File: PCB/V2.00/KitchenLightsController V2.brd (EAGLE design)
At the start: 100 x 90 mm, 116 parts, among them IC1 788TV, Q2 FDD8451, Q3 FDD8451, Q4 FDD8451, Q5 FDD8451, Q6 200mA/50V, U1 PHOTON_WITH_STACKABLE_HEADERS, U2 DS1820SOIC, U3 ACS712

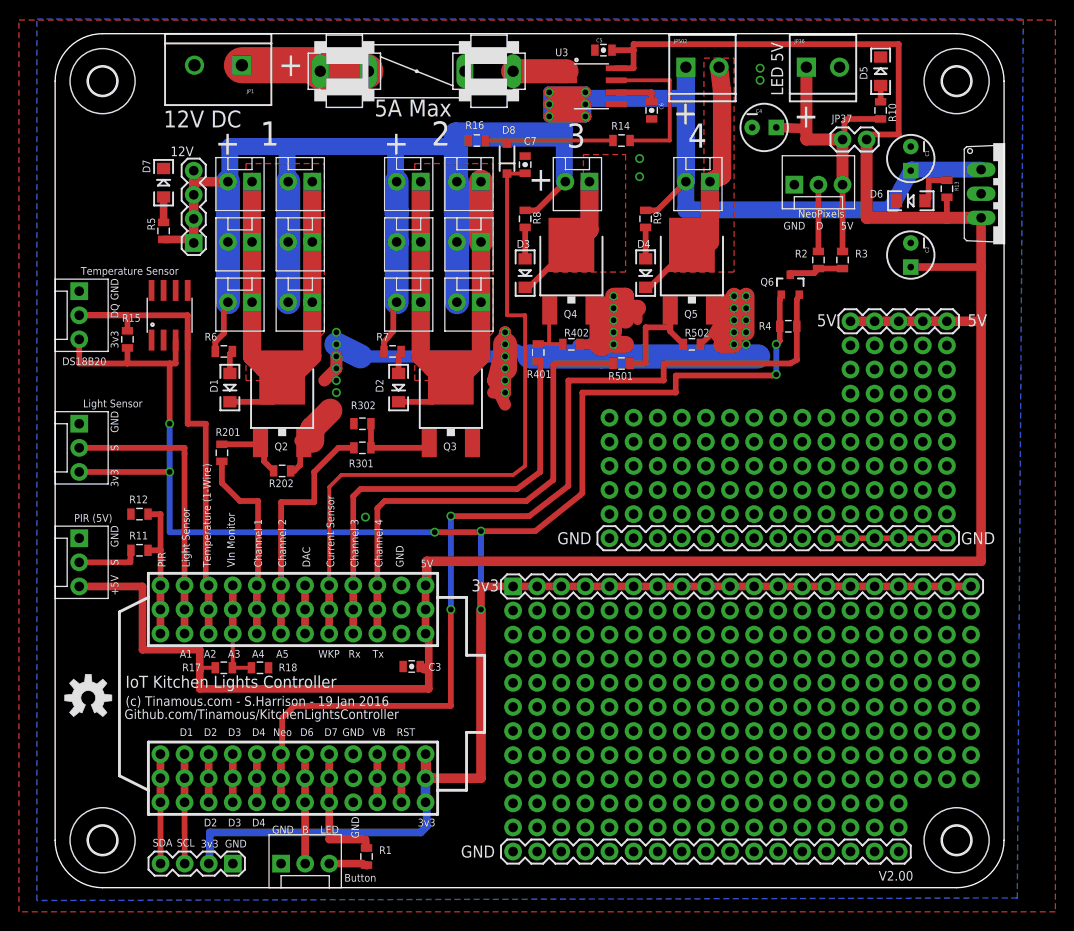
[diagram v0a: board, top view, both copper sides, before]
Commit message: Updated with minor tweaks and some additional component values specified from build of the v2.00 board.
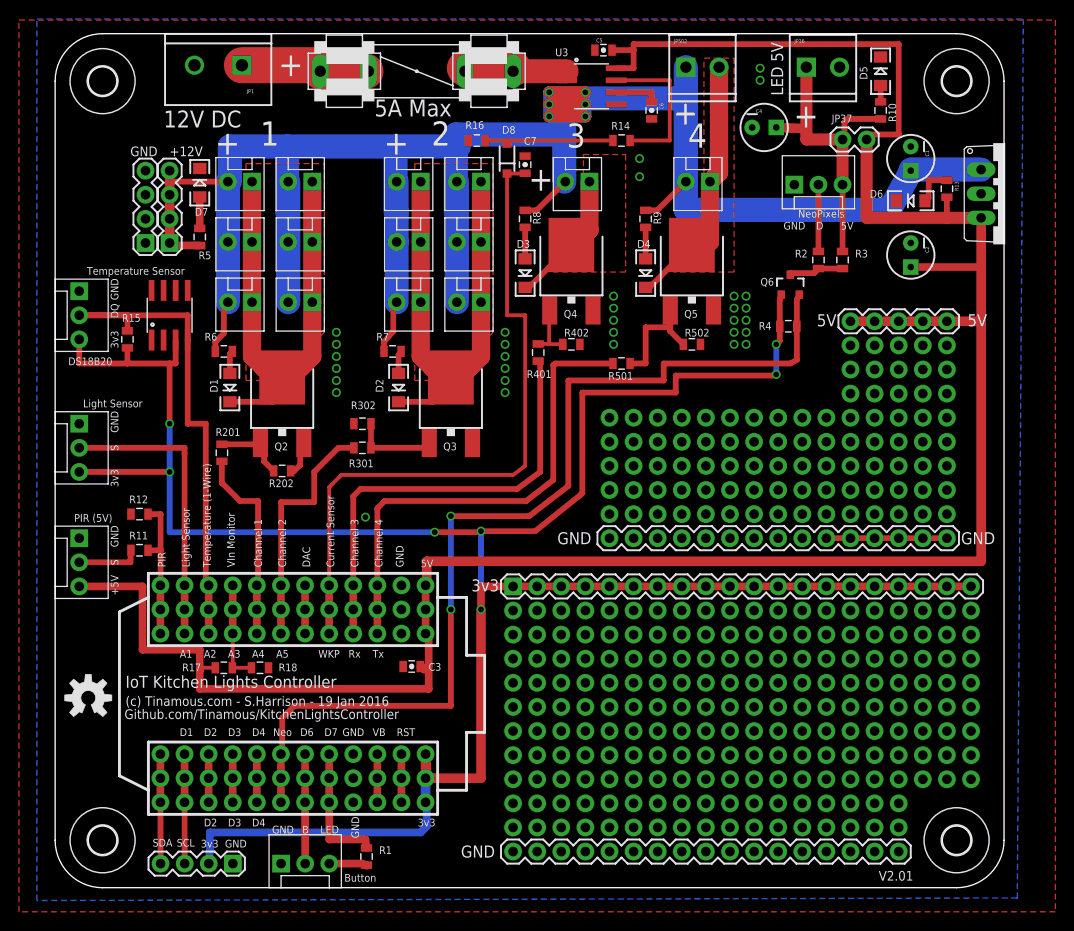
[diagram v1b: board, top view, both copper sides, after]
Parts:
- added JP41: (no value), SparkFun-Connectors:1X04
- C1, C2: value (none) -> 10uF 25V
- C3: value (none) -> 1uF
- C4: value (none) -> 220uF 16V
- D8: value (none) -> 1N4148W
- IC1: value 788TV -> 7805
- JP49: value Button -> Temperature
- Q6: value 200mA/50V -> BSS138
- R2: value 600R -> 330R
- R3: value 10R -> 4k7
- R4: value 10R -> DNP
- moved R5 3.86 mm to (15.2, 68.6)
- moved D7 3.81 mm to (15.2, 74.3)
- moved JP45 2.54 mm to (12.1, 67.9)
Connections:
- net GND: now also JP41.1, JP41.2, JP41.3, JP41.4
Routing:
- net GND: track 139.2 -> 16.4 mm
- net N$14: track 0.00 -> 5.08 mm
- net 12V: track 267.6 -> 270.0 mm
- net N$1: track 2.68 -> 3.31 mm
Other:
- board text added: "+12V"
- board text added: "V2.01"
- board text removed: "12V"
- board text removed: "V2.00"

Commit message: Corrected Gnd/+5V labels on NeoPixel connector which were the wrong way around.
Moved Via from area under Photon as it messed with the text.
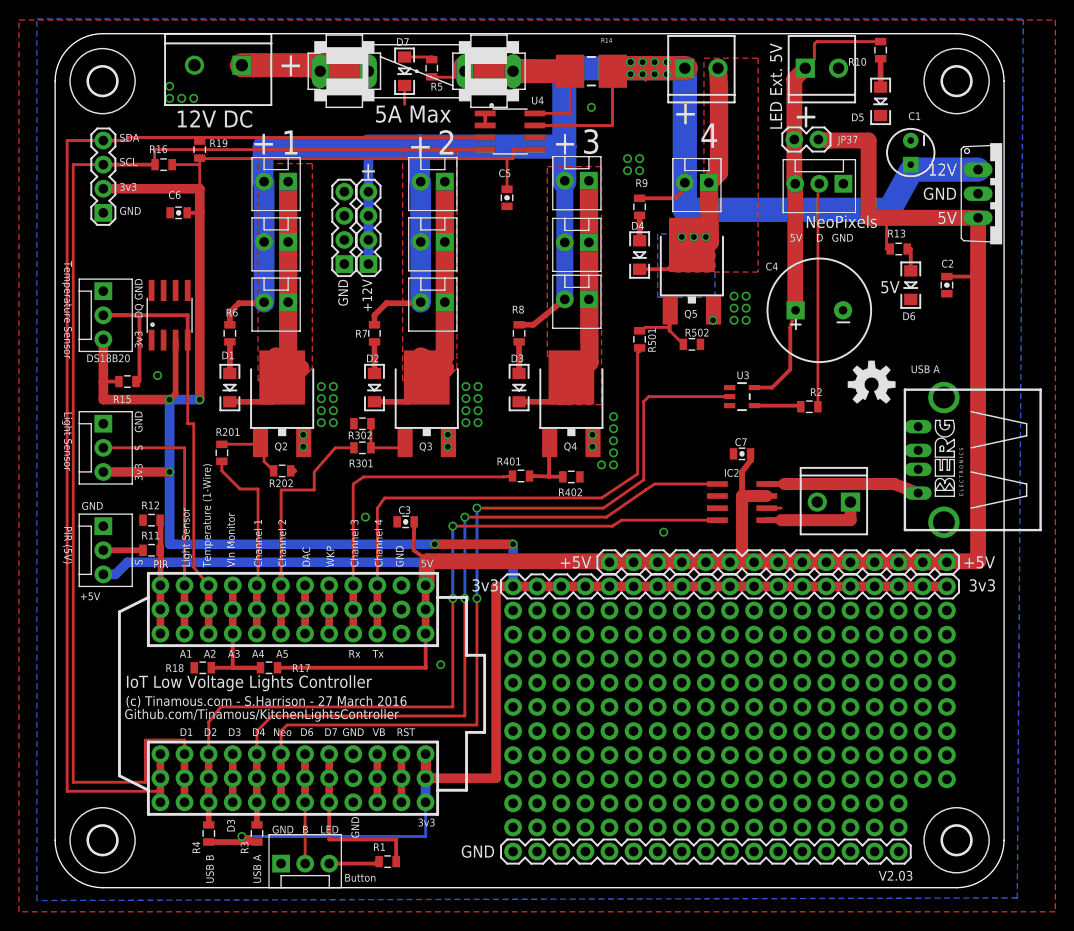
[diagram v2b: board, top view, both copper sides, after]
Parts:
- removed D8: 1N4148W, SparkFun-DiscreteSemi:SOD-123
- removed JP204, JP205, JP206, JP304, JP305, JP306: (no value), SparkFun-Connectors:MOLEX-1X2
- removed JP26, JP31, JP38, JP39, JP4, JP40: (no value), SparkFun-Connectors:1X08_NO_SILK
- removed JP29: (no value), SparkFun-Connectors:1X05
- removed JP3, JP5, JP7, JP8, JP9: (no value), SparkFun-Connectors:1X10_NO_SILK
- removed JP6: (no value), SparkFun-Connectors:1X15
- removed Q6: BSS138, SparkFun-DiscreteSemi:SOT23-3
- added IC2: LM3526M-L, SH-linear:SO08
- added JP402, JP403: (no value), SparkFun-Connectors:MOLEX-1X2
- added JP42: (no value), SparkFun-Connectors:1X15
- added JP43: 5V Out (USB B), SparkFun-Connectors:SCREWTERMINAL-3.5MM-2
- added R19: 4k7, SparkFun-Resistors:0805
- added U4: INA219AIDCNRSOIC, INA219AIDCNR:SO08
- added X2: PN87520-S, con-berg:PN87520-S
- C1: value 10uF 25V -> 330nF 50V
- C2: value 10uF 25V -> 1uF; device SparkFun-Capacitors:CPOL-RADIAL-10UF-25V -> SparkFun-Capacitors:0805-CAP
- C3: value 1uF -> 0.1uF
- C4: value 220uF 16V -> 1000uf/16V; device SparkFun-Capacitors:CPOL-RADIAL-10UF-25V -> SparkFun-Capacitors:CPOL-RADIAL-1000UF-25V-KIT
- C6: value 1nF -> 10uF
- C7: value 0.1uF -> 1uF
- JP32: device SparkFun-Connectors:1X20 -> SparkFun-Connectors:1X19
- JP36: value LED 5V -> LED Ext. 5V
- R14: value 2k -> 0.1; device SparkFun-Resistors:0805 -> SparkFun-Resistors:2512
- R16: value 10k -> 4k7
- R3: value 4k7 -> 10k
- R4: value DNP -> 10k
- U3: value ACS712 -> 74AHC1G125; device SparkFun-AnalogIC:SO08 -> SparkFun-DigitalIC:SOT23-5
- moved LOGO1 88.9 mm to (86.0, 53.0)
- moved R3 86.4 mm to (21.3, 5.71), turned to 270 degrees
- moved R4 81.2 mm to (16.2, 5.71), turned to 270 degrees
- moved JP2 69.9 mm to (5.08, 71.1), turned to 90 degrees
- moved C6 51.0 mm to (13.0, 71.1), turned to 0 degrees
- moved C7 38.1 mm to (72.4, 45.7), turned to 0 degrees
- moved U3 36.4 mm to (72.4, 51.8)
- moved R16 33.1 mm to (11.4, 76.2)
- moved R5 30.2 mm to (39.7, 86.4)
- moved D7 24.6 mm to (36.8, 86.0), turned to 270 degrees
- moved JP45 21.1 mm to (33.0, 65.7)
- moved JP41 21.1 mm to (30.5, 65.7)
- moved C4 20.1 mm to (80.5, 60.9), turned to 180 degrees
- moved C5 18.6 mm to (47.6, 72.7), turned to 90 degrees
- moved R2 15.5 mm to (79.5, 50.7), turned to 0 degrees
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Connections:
- net N$31 renamed CHANNEL_4_SWITCHED
- removed net CURRENT_SENSOR: C7.2, D8.C, U1.#5, U1.5, U1.@5
- removed net CURRENT_SENSOR_PRE: D8.A, R14.1, R16.1
- removed net D2: U1.#15, U1.15, U1.@15
- removed net D4: U1.#17, U1.17, U1.@17
- removed net N$13: Q6.3, R2.1, R3.1
- removed net N$15: C6.1, U3.6
- removed net N$28: D2.C, JP301.1, JP302.1, JP303.1, JP304.1, JP305.1, JP306.1, Q3.4
- removed net N$30: D3.C, JP401.1, Q4.4
- removed net N$9: D1.C, JP201.1, JP202.1, JP203.1, JP204.1, JP205.1, JP206.1, Q2.4
- new net CHANNEL_1_SWITCHED: D1.C, JP201.1, JP202.1, JP203.1, Q2.4
- new net CHANNEL_2_SWITCHED: D2.C, JP301.1, JP302.1, JP303.1, Q3.4
- new net CHANNEL_3_SWITCHED: D3.C, JP401.1, JP402.1, JP403.1, Q4.4
- new net USB_VA: IC2.8, X2.1
- new net USB_VB: IC2.5, JP43.1
- new net USB_VENABLE_A: IC2.1, R3.1, U1.#17, U1.17, U1.@17
- new net USB_VENABLE_B: IC2.4, R4.1, U1.#15, U1.15, U1.@15
- new net WKP: U1.#5, U1.5, U1.@5
- net 12V: now also JP402.2, JP403.2, R14.2, U4.7; no longer JP204.2, JP205.2, JP206.2, JP304.2, JP305.2, JP306.2, R5.2, U3.3, U3.4
- net 3.3V: now also C5.2, C6.2, R16.1, R19.1, R3.2, U4.5; no longer JP32.20, Q6.1
- net 5V: now also C2.2, C7.2, IC2.7, JP42.1, JP42.10, JP42.11, JP42.12, JP42.13, JP42.14, JP42.15, JP42.2, JP42.3, JP42.4, JP42.5, JP42.6, JP42.7, JP42.8, JP42.9; no longer C2.1, C5.2, JP29.1, JP29.2, JP29.3, JP29.4, JP29.5, U3.8
- net GND: now also C2.1, C4.-, C6.1, IC2.6, JP43.2, U3.1, U3.3, U4.1, U4.2, U4.6, X2.4, X2.S1, X2.S2; no longer C2.2, C4.2, C6.2, JP6.1, JP6.10, JP6.11, JP6.12, JP6.13, JP6.14, JP6.15, JP6.2, JP6.3, JP6.4, JP6.5, JP6.6, JP6.7, JP6.8, JP6.9, R16.2, U3.5
- net N$5: now also R14.1, R5.2, U4.8; no longer U3.1, U3.2
- net N$6: now also R2.1, U3.4; no longer R14.2, U3.7
- net NEOPIXELS: now also U3.2; no longer Q6.2, R4.1
- net SCL: now also R16.2, U4.4
- net SDA: now also R19.2, U4.3
- net VIN: now also C4.+, U3.5; no longer C4.1, R3.2
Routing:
- net SCL: track 11.5 -> 138.0 mm
- net SDA: track 11.5 -> 132.2 mm
- net USB_VENABLE_B: track 0.00 -> 84.5 mm, vias 0 -> 2
- net USB_VENABLE_A: track 0.00 -> 81.1 mm, vias 0 -> 2
- net CURRENT_SENSOR: track 71.6 -> 0.00 mm
- net N$9: track 54.1 -> 0.00 mm
- net N$28: track 52.0 -> 0.00 mm
- net 12V: track 270.0 -> 224.9 mm, vias 6 -> 9
- net CHANNEL_1_SWITCHED: track 0.00 -> 36.8 mm
- net CHANNEL_2_SWITCHED: track 0.00 -> 35.0 mm
- net CHANNEL_3_SWITCHED: track 0.00 -> 29.5 mm
- net 3.3V: track 253.0 -> 281.3 mm, vias 7 -> 6
- net N$5: track 5.64 -> 29.2 mm
- net NEOPIXELS: track 104.8 -> 87.3 mm
- net N$8: track 7.04 -> 23.6 mm
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- added copper zone on layer 1, net CHANNEL_1_SWITCHED
- added copper zone on layer 1, net CHANNEL_2_SWITCHED
- added copper zone on layer 1, net CHANNEL_3_SWITCHED
- added copper zone on layer 16, net CHANNEL_4_SWITCHED
- removed copper zone on layer 1, net N$28
- removed copper zone on layer 1, net N$30
- removed copper zone on layer 1, net N$9
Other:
- board text added: "(c) Tinamous.com - S.Harrison - 27 March 2016"
- board text added: "12V"
- board text added: "IoT Low Voltage Lights Controller"
- board text added: "USB A"
- board text added: "USB B"
- board text added: "V2.03"
- board text removed: "(c) Tinamous.com - S.Harrison - 19 Jan 2016"
- board text removed: "Current Sensor"
- board text removed: "IoT Kitchen Lights Controller"
- board text removed: "V2.01"
